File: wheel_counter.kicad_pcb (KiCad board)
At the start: 2 copper layers, 99.6 x 98 mm, 112 parts, among them J2 Conn_01x02_Pin, U2 IRLML6344TRPBF, U3 IRLML6344TRPBF

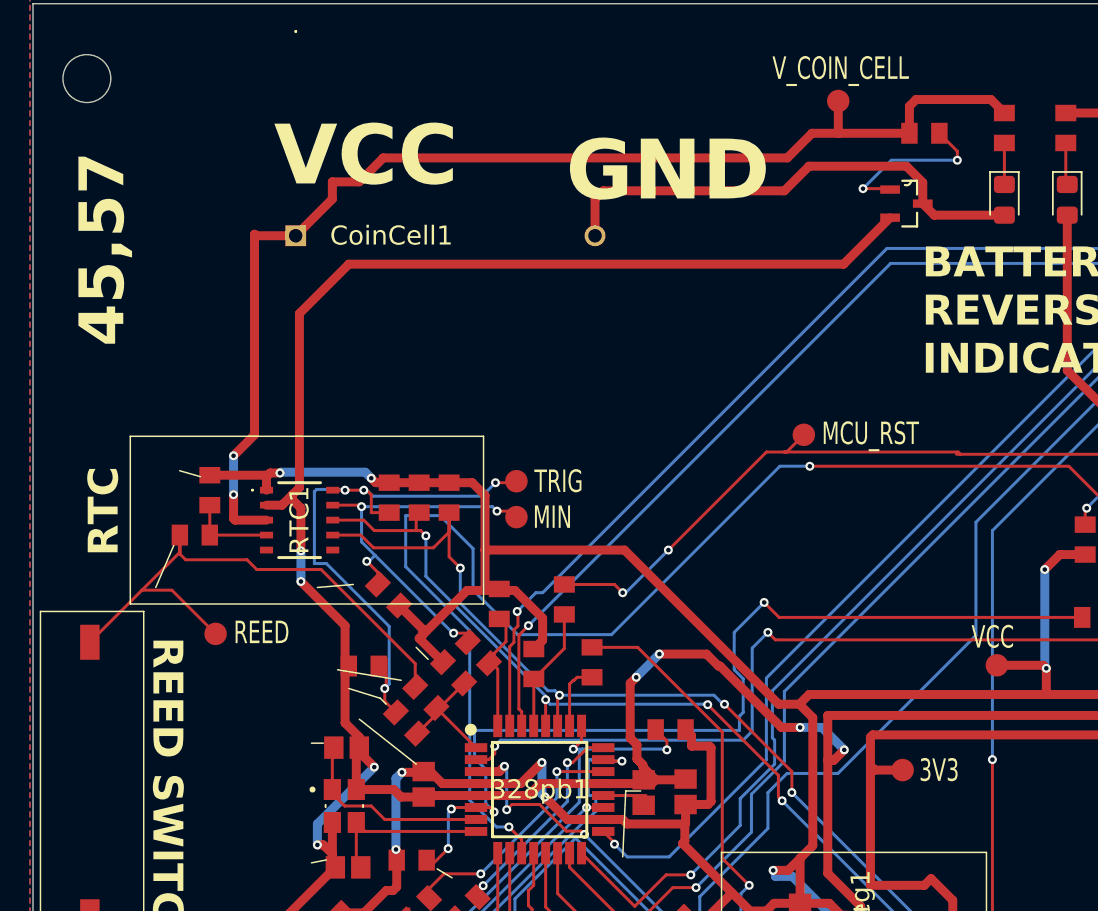
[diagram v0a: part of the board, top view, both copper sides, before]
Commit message: fix ground
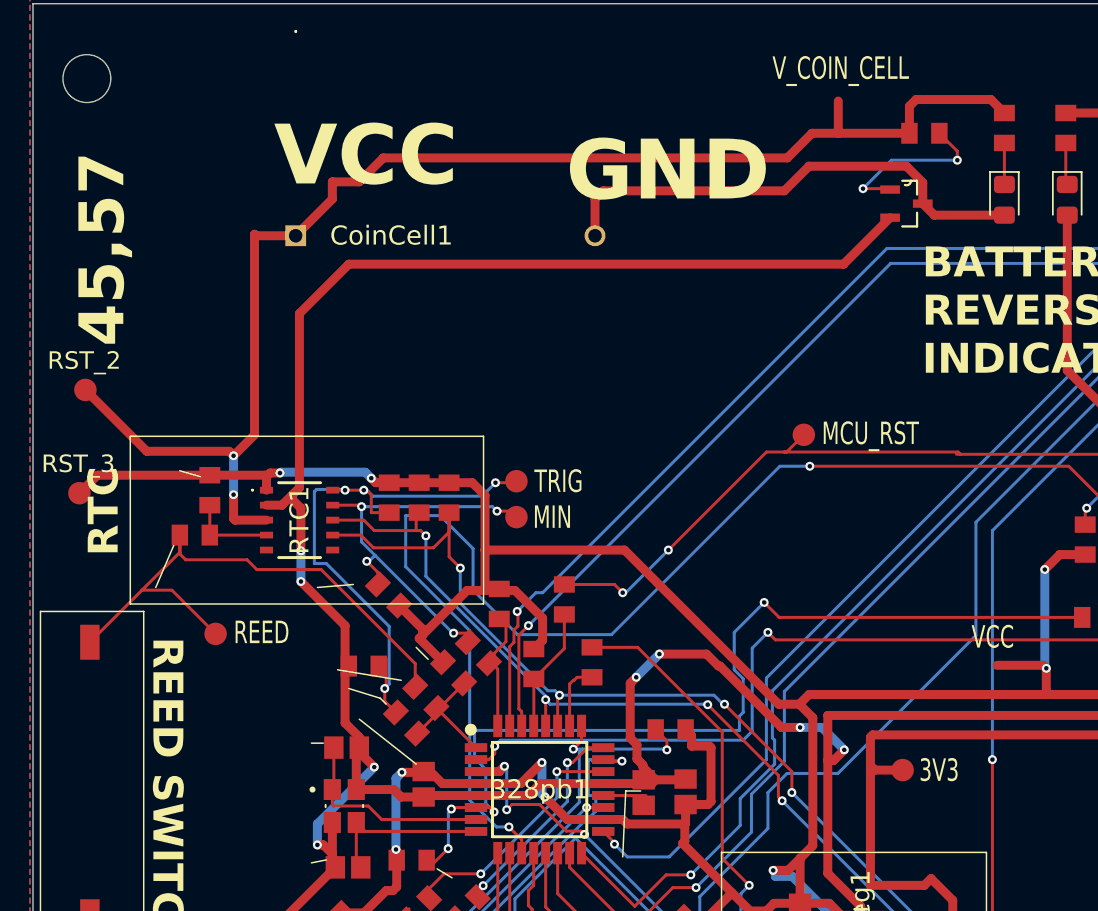
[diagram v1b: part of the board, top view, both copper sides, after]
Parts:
- removed VBAT_1, VCC_1: ~, ishan:MOX-OXLEY-TEST-POINT
- added RST_2: ~, ishan:MOX-OXLEY-TEST-POINT, F.Cu at (39.9, 77.8)
- added RST_3: ~, ishan:MOX-OXLEY-TEST-POINT, F.Cu at (39.5, 84.7)
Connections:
- 328pb1 pad 7: GND -> Net-(328pb1-(XTAL1/TOSC1)_PB6)
- C_XTAL1 pad 1: GND -> Net-(328pb1-(XTAL1/TOSC1)_PB6)
- Y1 pad 1: GND -> Net-(328pb1-(XTAL1/TOSC1)_PB6)
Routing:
- net Net-(328pb1-(XTAL1/TOSC1)_PB6): track 0.00 -> 13.9 mm
- net GND: track 473.4 -> 460.4 mm
- net VBAT: track 80.0 -> 91.7 mm
- net VCC: track 333.0 -> 342.2 mm
